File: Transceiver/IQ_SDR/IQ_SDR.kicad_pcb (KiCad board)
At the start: 2 copper layers, 100 x 100 mm, 116 parts, among them CON1 SJ1-3523N, J1 ANT, J10 LO_I, J11 LO_Q, J12 GNDA, J13 I_IN, J14 Q_IN, J15 +5V, J16 4.3V, J17 I_OUT, J18 Q_OUT, J19 Conn_01x01_Male, J2 GND, J20 Conn_01x01_Male, J3 V_IN pin header, J4 GND, J5 V_IN, J6 FIL_O, J7 CLK1, J8 CLK2, J9 CLK0, P1 BNC, P2 SMA, Q1 MMBT2222A-TP, T1 Transformer_1P_SS, U1 FST3253, U2 Si5351A-B-GT, U3 TS5A23157, U4 LM4562 or LT6231, U5 74ALVC74D, Y1 CX3225

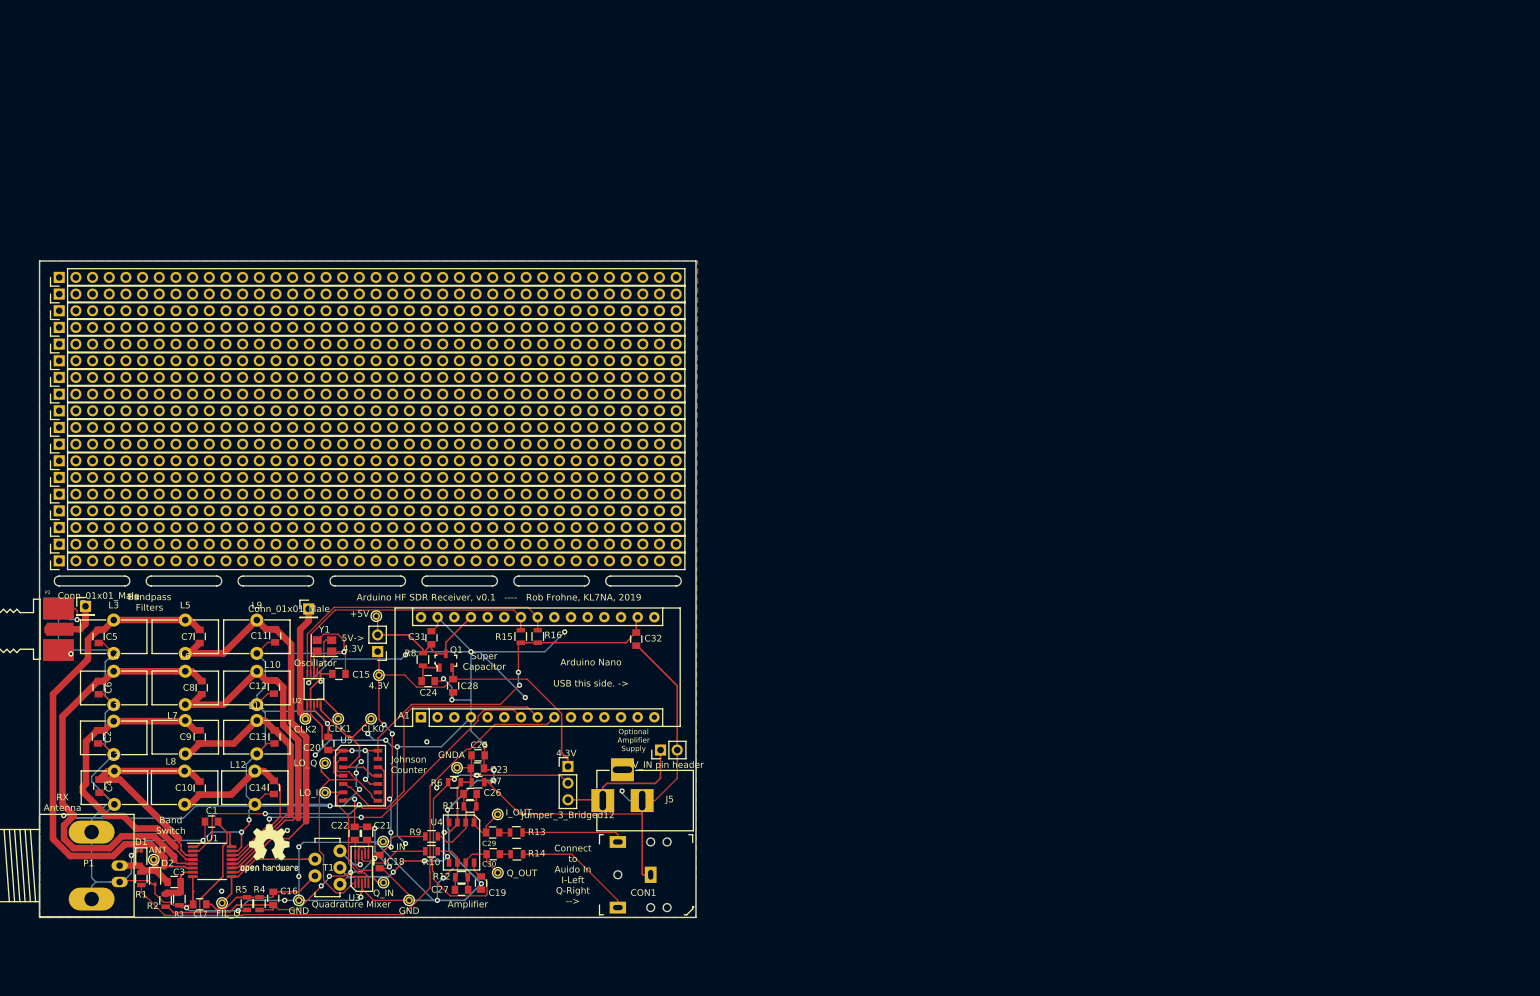
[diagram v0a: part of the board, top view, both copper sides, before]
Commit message: Further change to schematic and moving simulations
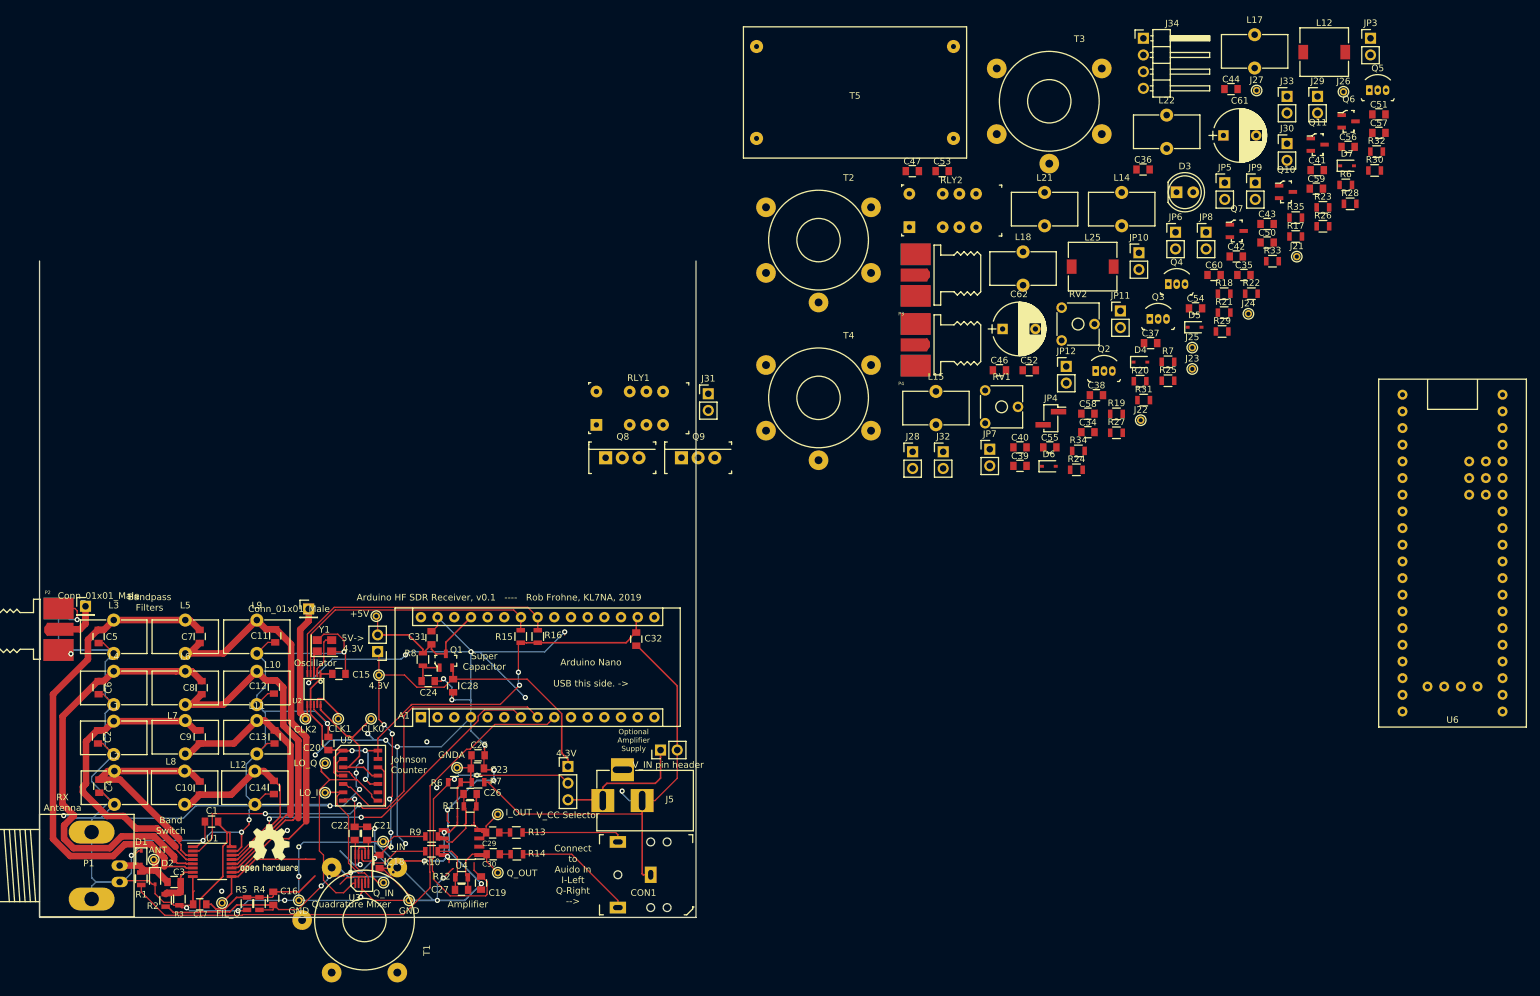
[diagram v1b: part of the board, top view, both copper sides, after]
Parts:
- removed REF** (x18): Pin_Header_Straight_1x38_Pitch2.54mm, Pin_Headers:Pin_Header_Straight_1x38_Pitch2.54mm
- added C34: 82pF, Capacitors_SMD:C_0805, F.Cu at (254.7, 71.1)
- added C35: 1uF, Capacitors_SMD:C_0805, F.Cu at (278.5, 47.1)
- added C36: 10uF, Capacitors_SMD:C_0805, F.Cu at (263.1, 31.1)
- added C37: 1u, Capacitors_SMD:C_0805, F.Cu at (264.3, 57.5)
- added C38: 510pF, Capacitors_SMD:C_0805, F.Cu at (256.0, 65.4)
- added C39: 330pF, Capacitors_SMD:C_0805, F.Cu at (244.4, 76.2)
- added C40: 0.1uF, Capacitors_SMD:C_0805, F.Cu at (244.4, 73.4)
- added C41: 220pF, Capacitors_SMD:C_0805, F.Cu at (289.6, 31.2)
- added C42: 680pF, Capacitors_SMD:C_0805, F.Cu at (277.3, 44.3)
- added C43: 330pF, Capacitors_SMD:C_0805, F.Cu at (282.0, 39.4)
- added C44: 220pF, Capacitors_SMD:C_0805, F.Cu at (276.5, 18.8)
- added C46: 180pF, Capacitors_SMD:C_0805, F.Cu at (241.2, 61.6)
- added C47: 82pF, Capacitors_SMD:C_0805, F.Cu at (228.0, 31.3)
- added C50: 0.1uF, Capacitors_SMD:C_0805, F.Cu at (282.0, 42.2)
- added C51: 0.1uF, Capacitors_SMD:C_0805, F.Cu at (299.0, 22.7)
- added C52: 0.1uF, Capacitors_SMD:C_0805, F.Cu at (245.8, 61.6)
- added C53: 0.1uF, Capacitors_SMD:C_0805, F.Cu at (232.5, 31.3)
- added C54: 0.1uF, Capacitors_SMD:C_0805, F.Cu at (271.1, 52.2)
- added C55: 0.1uF, Capacitors_SMD:C_0805, F.Cu at (248.9, 73.4)
- added C56: 0.1uF, Capacitors_SMD:C_0805, F.Cu at (294.3, 27.6)
- added C57: 0.1uF, Capacitors_SMD:C_0805, F.Cu at (299.0, 25.5)
- added C58: 0.1uF, Capacitors_SMD:C_0805, F.Cu at (254.7, 68.3)
- added C59: 0.1uF, Capacitors_SMD:C_0805, F.Cu at (289.5, 34.0)
- added C60: 0.1uF, Capacitors_SMD:C_0805, F.Cu at (273.9, 47.1)
- added C61: 470uF, Capacitors_THT:CP_Radial_D8.0mm_P5.00mm, F.Cu at (275.3, 25.9)
- added C62: 470uF, Capacitors_THT:CP_Radial_D8.0mm_P5.00mm, F.Cu at (241.7, 55.4)
- added D3: LED_Solid, LEDs:LED_D5.0mm, F.Cu at (268.2, 34.5)
- added D4: 1N914, Diodes_SMD:D_SOD-323, F.Cu at (262.7, 60.4)
- added D5: 1N914, Diodes_SMD:D_SOD-323, F.Cu at (271.0, 55.1)
- added D6: 1N914, Diodes_SMD:D_SOD-323, F.Cu at (248.8, 76.3)
- added D7: 1N914, Diodes_SMD:D_SOD-323, F.Cu at (294.2, 30.5)
- added J21: V_CC, Connectors:PINTST, F.Cu at (286.5, 44.3)
- added J22: Ba, Connectors:PINTST, F.Cu at (262.8, 69.3)
- added J23: Bb, Connectors:PINTST, F.Cu at (270.6, 61.4)
- added J24: Cb, Connectors:PINTST, F.Cu at (279.2, 53.0)
- added J25: Ca, Connectors:PINTST, F.Cu at (270.6, 58.2)
- added J26: Gb, Connectors:PINTST, F.Cu at (293.6, 19.2)
- added J27: Ga, Connectors:PINTST, F.Cu at (280.4, 19.0)
- added J28: Conn_01x02_Female, Socket_Strips:Socket_Strip_Straight_1x02_Pitch2.54mm, F.Cu at (228.0, 74.1)
- added J29: Conn_01x02_Female, Socket_Strips:Socket_Strip_Straight_1x02_Pitch2.54mm, F.Cu at (289.7, 19.9)
- added J30: Conn_01x02_Female, Socket_Strips:Socket_Strip_Straight_1x02_Pitch2.54mm, F.Cu at (285.0, 27.1)
- added J31: Conn_01x02_Female, Socket_Strips:Socket_Strip_Straight_1x02_Pitch2.54mm, F.Cu at (196.9, 65.2)
- added J32: Conn_01x02_Female, Socket_Strips:Socket_Strip_Straight_1x02_Pitch2.54mm, F.Cu at (232.7, 74.1)
- added J33: Conn_01x02_Female, Socket_Strips:Socket_Strip_Straight_1x02_Pitch2.54mm, F.Cu at (285.0, 19.9)
- added J34: Conn_01x04_Male, Pin_Headers:Pin_Header_Angled_1x04_Pitch2.54mm, F.Cu at (263.2, 11.1)
- added JP10: BP_2, Pin_Headers:Pin_Header_Straight_1x02_Pitch2.54mm, F.Cu at (262.5, 43.8)
- added JP11: Tx filter disconnect, Pin_Headers:Pin_Header_Straight_1x02_Pitch2.54mm, F.Cu at (259.7, 52.6)
- added JP12: 40m Filter Bypass, Pin_Headers:Pin_Header_Straight_1x02_Pitch2.54mm, F.Cu at (251.4, 61.1)
- added JP3: Ground loop mitigation for the Arduino, Pin_Headers:Pin_Header_Straight_1x02_Pitch2.54mm, F.Cu at (297.8, 11.1)
- added JP4: Ground loop mitigation for the RX antenna, Pin_Headers:Pin_Header_Straight_1x02_Pitch2.00mm_SMD_Pin1Right, F.Cu at (249.1, 69.0)
- added JP5: T2 bypass, Pin_Headers:Pin_Header_Straight_1x02_Pitch2.54mm, F.Cu at (275.6, 33.1)
- added JP6: T2 bypass, Pin_Headers:Pin_Header_Straight_1x02_Pitch2.54mm, F.Cu at (268.1, 40.6)
- added JP7: V_IN ground loop mitigation, Pin_Headers:Pin_Header_Straight_1x02_Pitch2.54mm, F.Cu at (239.8, 73.7)
- added JP8: Ground loop mitigation for audio, Pin_Headers:Pin_Header_Straight_1x02_Pitch2.54mm, F.Cu at (272.7, 40.6)
- added JP9: BP_1, Pin_Headers:Pin_Header_Straight_1x02_Pitch2.54mm, F.Cu at (280.2, 33.1)
- added L12: 300uH, Inductors_SMD:L_7.3x7.3_H4.5, F.Cu at (290.7, 13.2)
- added L14: 590nH, Inductors_THT:L_Toroid_Vertical_L10.0mm_W5.0mm_P5.08mm, F.Cu at (259.9, 34.6)
- added L15: 2.4uH, Inductors_THT:L_Toroid_Vertical_L10.0mm_W5.0mm_P5.08mm, F.Cu at (231.6, 64.9)
- added L17: 1.7uH, Inductors_THT:L_Toroid_Vertical_L10.0mm_W5.0mm_P5.08mm, F.Cu at (280.1, 10.5)
- added L18: 910nH, Inductors_THT:L_Toroid_Vertical_L10.0mm_W5.0mm_P5.08mm, F.Cu at (244.8, 43.6)
- added L21: 1.24uH, Inductors_THT:L_Toroid_Vertical_L10.0mm_W5.0mm_P5.08mm, F.Cu at (248.1, 34.6)
- added L22: 590nH, Inductors_THT:L_Toroid_Vertical_L10.0mm_W5.0mm_P5.08mm, F.Cu at (266.7, 22.8)
- added L25: 300uH, Inductors_SMD:L_7.3x7.3_H4.5, F.Cu at (255.4, 45.9)
- added P3: SMA, SMA:SMA_EDGE, F.Cu at (237.4, 47.1)
- added P4: SMA, SMA:SMA_EDGE, F.Cu at (237.4, 57.8)
- added Q10: MMBT2222A-TP, digikey-footprints:SOT-23-3, F.Cu at (284.9, 34.5)
- added Q11: MMBT2222A-TP, digikey-footprints:SOT-23-3, F.Cu at (289.7, 27.3)
- added Q2: 2N3904, digikey-footprints:TO-92-3, F.Cu at (255.9, 61.8)
- added Q3: 2N3904, digikey-footprints:TO-92-3, F.Cu at (264.1, 53.8)
- added Q4: 2N3904, digikey-footprints:TO-92-3, F.Cu at (267.0, 48.5)
- added Q5: 2N3904, digikey-footprints:TO-92-3, F.Cu at (297.6, 19.0)
- added Q6: MMBT2222A-TP, digikey-footprints:SOT-23-3, F.Cu at (294.4, 23.7)
- added Q7: MMBT2222A-TP, digikey-footprints:SOT-23-3, F.Cu at (277.4, 40.4)
- added Q8: IRF510PBF, digikey-footprints:TO-220-3, F.Cu at (181.2, 75.0)
- added Q9: IRF510PBF, digikey-footprints:TO-220-3, F.Cu at (192.8, 75.0)
- added R17: 100, Resistors_SMD:R_0805, F.Cu at (286.4, 41.3)
- added R18: 100, Resistors_SMD:R_0805, F.Cu at (275.5, 50.0)
- added R19: 22, Resistors_SMD:R_0805, F.Cu at (259.1, 68.3)
- added R20: 22, Resistors_SMD:R_0805, F.Cu at (262.7, 63.3)
- added R21: 1k, Resistors_SMD:R_0805, F.Cu at (275.5, 52.9)
- added R22: 1k, Resistors_SMD:R_0805, F.Cu at (279.6, 50.0)
- added R23: 22, Resistors_SMD:R_0805, F.Cu at (290.5, 36.8)
- added R24: 22, Resistors_SMD:R_0805, F.Cu at (253.0, 76.8)
- added R25: 2.2, Resistors_SMD:R_0805, F.Cu at (266.9, 63.2)
- added R26: 0, Resistors_SMD:R_0805, F.Cu at (290.5, 39.7)
- added R27: 0, Resistors_SMD:R_0805, F.Cu at (259.1, 71.2)
- added R28: 500, Resistors_SMD:R_0805, F.Cu at (294.7, 36.3)
- added R29: 47, Resistors_SMD:R_0805, F.Cu at (275.2, 55.7)
- added R30: 47, Resistors_SMD:R_0805, F.Cu at (298.4, 31.2)
- added R31: 220, Resistors_SMD:R_0805, F.Cu at (263.2, 66.2)
- added R32: 220, Resistors_SMD:R_0805, F.Cu at (298.7, 28.3)
- added R33: 4.7k, Resistors_SMD:R_0805, F.Cu at (282.8, 45.0)
- added R34: 4.7k, Resistors_SMD:R_0805, F.Cu at (253.3, 73.9)
- added R35: 1.6k, Resistors_SMD:R_0805, F.Cu at (286.4, 38.4)
- added R6: 2k, Resistors_SMD:R_0805, F.Cu at (294.0, 33.4)
- added R7: 27k, Resistors_SMD:R_0805, F.Cu at (266.9, 60.4)
- added RLY1: TX2SA-L-3V-Z, IQ_SDR:TX2SA-L-3V-Z, F.Cu at (179.8, 64.9)
- added RLY2: TX2SA-L-3V-Z, IQ_SDR:TX2SA-L-3V-Z, F.Cu at (227.5, 34.8)
- added RV1: 10k, Potentiometers:Potentiometer_Trimmer_ACP_CA6v_Horizontal, F.Cu at (239.1, 69.7)
- added RV2: 10k, Potentiometers:Potentiometer_Trimmer_ACP_CA6v_Horizontal, F.Cu at (250.7, 57.1)
- added T2: Transformer_1P_1S, IQ_SDR:Transformer_Toroid_Tapped_Secondary_Horizontal_D14.0mm_Amidon-T50, F.Cu at (205.7, 46.8)
- added T3: Transformer_1P_1S, IQ_SDR:Transformer_Toroid_Tapped_Secondary_Horizontal_D14.0mm_Amidon-T50, F.Cu at (240.8, 25.7)
- added T4: Transformer_SP_1S, IQ_SDR:Transformer_Toroid_Tapped_Secondary_Horizontal_D14.0mm_Amidon-T50, F.Cu at (205.7, 70.8)
- added T5: BN43-6802, IQ_SDR:BN43-6802, F.Cu at (219.2, 19.3)
- added U6: Blue Pill, blue_pill:BLUEPILL, F.Cu at (310.2, 89.5)
- C21, C22: value 0.1uF -> 0.02uF
- C26, C27: value 2200pF -> 50pF
- JP2: value Jumper_3_Bridged12 -> V_CC Selector
- L10: value 497nH -> 626nH
- L11: value 1uH -> 1.7uH
- L9: value 232nH -> 256nH
- R10, R9: value 10 -> 50
- R11, R12: value 1.0k -> 13k
- T1: footprint SMA:4_to_1_Transmission_Line_TransformerTHT -> IQ_SDR:Transformer_Toroid_Tapped_Secondary_Horizontal_D14.0mm_Amidon-T50
- U1: value FST3253 -> FST3253 or TS3A5017
- U4: footprint SMA:DMP8 -> Housings_SOIC:SOIC-8_3.9x4.9mm_Pitch1.27mm
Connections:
- A1 pad 29: GND -> /D_GND
- A1 pad 4: GND -> /D_GND
- C16 pad 2: Net-(C16-Pad2) -> GNDA
- C17 pad 1: Net-(C16-Pad2) -> GNDA
- C23 pad 2: GNDA -> Net-(C23-Pad2)
- C3 pad 1: /RF_IN -> Net-(C3-Pad1)
- C4 pad 1: Net-(C10-Pad2) -> Net-(C4-Pad1)
- C7 pad 2: Net-(C5-Pad1) -> Net-(C7-Pad2)
- C8 pad 2: Net-(C6-Pad1) -> Net-(C8-Pad2)
- C9 pad 2: Net-(C2-Pad1) -> Net-(C9-Pad2)
- CON1 pad 1: GND -> Net-(CON1-Pad1)
- D1 pad 2: /RF_IN -> Net-(C3-Pad1)
- D2 pad 1: /RF_IN -> Net-(C3-Pad1)
- J1 pad 1: /RF_IN -> Net-(C3-Pad1)
- J3 pad 2: GND -> Net-(J3-Pad2)
- J5 pad 2: GND -> Net-(J3-Pad2)
- L1 pad 2: GND -> GNDA
- L10 pad 2: GND -> GNDA
- L11 pad 2: GND -> GNDA
- L2 pad 1: Net-(C10-Pad2) -> Net-(C4-Pad1)
- L2 pad 2: GND -> GNDA
- L3 pad 2: GND -> GNDA
- L4 pad 2: GND -> GNDA
- L5 pad 2: Net-(C11-Pad1) -> Net-(C7-Pad2)
- L6 pad 2: Net-(C12-Pad1) -> Net-(C8-Pad2)
- L7 pad 2: Net-(C13-Pad1) -> Net-(C9-Pad2)
- L8 pad 1: Net-(C10-Pad2) -> Net-(C4-Pad1)
- L8 pad 2: Net-(C10-Pad1) -> Net-(C10-Pad2)
- L9 pad 2: GND -> GNDA
- P1 pad 1: /RF_IN -> Net-(P1-Pad1)
- P1 pad 2: GND -> Net-(P1-Pad2)
- R1 pad 1: /RF_IN -> Net-(C3-Pad1)
- R4 pad 1: Net-(C16-Pad2) -> GNDA
- R5 pad 2: Net-(C16-Pad2) -> GNDA
- T1 pad 1: Net-(C16-Pad2) -> GNDA
- T1 pad 3: Net-(T1-Pad3) -> Net-(R26-Pad2)
- T1 pad 5: Net-(T1-Pad5) -> Net-(R27-Pad2)
- U1 pad 3: Net-(C10-Pad2) -> Net-(C4-Pad1)
- U1 pad 9: Net-(J6-Pad1) -> Net-(JP9-Pad1)
- U3 pad 2: Net-(T1-Pad5) -> Net-(R27-Pad1)
- U3 pad 4: Net-(T1-Pad5) -> Net-(R27-Pad1)
- U3 pad 7: Net-(T1-Pad3) -> Net-(R26-Pad1)
- U3 pad 9: Net-(T1-Pad3) -> Net-(R26-Pad1)
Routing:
- net Net-(C16-Pad2): track 19.3 -> 0.00 mm
- net GNDA: track 40.6 -> 60.0 mm
- net Net-(T1-Pad3): track 8.53 -> 0.00 mm, vias 1 -> 0
- net Net-(R26-Pad1): track 0.00 -> 8.53 mm, vias 0 -> 1
- net Net-(T1-Pad5): track 6.86 -> 0.00 mm
- net Net-(R27-Pad1): track 0.00 -> 6.86 mm
- removed copper zone on B.Cu, net GND
- removed copper zone on F.Cu, net GND
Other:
- outline, holes or cut-outs redrawn

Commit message: PCB initial design
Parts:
- removed the L12 at (127.8, 122.7)
- removed the R6 at (158.2, 124.4)
- removed the R7 at (161.8, 124.4)
- removed REF***: OSHW-Logo2_36.5x30mm_SilkScreen, Symbols:OSHW-Logo2_36.5x30mm_SilkScreen
- removed REF***: OSHW-Logo2_9.8x8mm_SilkScreen, Symbols:OSHW-Logo2_9.8x8mm_SilkScreen
- added JP13: QRP, Pin_Headers:Pin_Header_Straight_1x02_Pitch2.54mm, F.Cu at (106.0, 75.5)
- added JP14: QRP, Pin_Headers:Pin_Header_Straight_1x02_Pitch2.54mm, F.Cu at (135.0, 75.8)
- added P5: SMA, SMA:SMA_EDGE, F.Cu at (88.8, 83.2)
- J34: footprint Pin_Headers:Pin_Header_Angled_1x04_Pitch2.54mm -> Pin_Headers:Pin_Header_Straight_1x04_Pitch2.54mm
- JP4: footprint Pin_Headers:Pin_Header_Straight_1x02_Pitch2.00mm_SMD_Pin1Right -> Pin_Headers:Pin_Header_Straight_1x02_Pitch2.54mm
- R26, R27: footprint Resistors_SMD:R_0805 -> Socket_Strips:Socket_Strip_Straight_1x02_Pitch2.54mm
- T1, T4: footprint IQ_SDR:Transformer_Toroid_Tapped_Secondary_Horizontal_D14.0mm_Amidon-T50 -> IQ_SDR:T50-2_vertical_5_pin
- T2, T3: footprint IQ_SDR:Transformer_Toroid_Tapped_Secondary_Horizontal_D14.0mm_Amidon-T50 -> IQ_SDR:T50-2_vertical_4_pin
- moved Q5 198.0 mm to (111.8, 87.2), turned to 270 degrees
- moved R23 192.6 mm to (107.5, 96.8), turned to 180 degrees
- moved L12 191.9 mm to (102.2, 49.5), turned to 180 degrees
- moved JP9 191.0 mm to (122.2, 140.5), turned to 270 degrees
- moved C57 190.7 mm to (110.0, 50.8)
- moved J21 190.3 mm to (96.2, 47.2)
- moved J27 187.6 mm to (96.2, 54.8)
- moved C51 186.1 mm to (125.2, 89.2), turned to 90 degrees
- moved J29 181.4 mm to (152.2, 138.2), turned to 90 degrees
- moved R17 181.2 mm to (113.5, 95.8), turned to 270 degrees
- moved R26 178.8 mm to (144.8, 143.2), turned to 270 degrees
- moved C41 178.3 mm to (122.2, 92.5)
- moved J33 176.5 mm to (158.5, 143.0), turned to 90 degrees
- moved C61 175.8 mm to (104.2, 66.5), turned to 180 degrees
- moved C60 175.0 mm to (100.8, 72.5), turned to 180 degrees
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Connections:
- net Net-(C34-Pad1) renamed /Rfe
- net Net-(C35-Pad2) renamed /RFc
- net Net-(C38-Pad1) renamed /RFg
- net Net-(C39-Pad1) renamed /RFf
- net Net-(C42-Pad1) renamed /RFk
- net Net-(C43-Pad1) renamed /RFj
- net Net-(C46-Pad1) renamed /RFh
- net Net-(C47-Pad1) renamed /RFd
- net Net-(P1-Pad1) renamed /RFm
- net Net-(P1-Pad2) renamed /RFb
- net Net-(P4-Pad2) renamed /RFa
- A1 pad 25: (no net) -> /TX_BAND
- A1 pad 26: (no net) -> /ANT_RLY
- L12 pad 1: Net-(L12-Pad1) -> /PA_V_CCb
- L25 pad 1: Net-(L25-Pad1) -> /PA_V_CCc
- Q3 pad 1: Net-(C44-Pad1) -> Net-(Q3-Pad1)
- Q3 pad 3: Net-(Q3-Pad3) -> Net-(C44-Pad1)
- Q5 pad 1: Net-(C44-Pad1) -> Net-(Q5-Pad1)
- Q5 pad 3: Net-(Q5-Pad3) -> Net-(C44-Pad1)
- Q8 pad 2: Net-(Q8-Pad2) -> /PA_V_CCb
- Q9 pad 2: Net-(Q9-Pad2) -> /PA_V_CCc
- R15 pad 1: /SCL -> /SDA
- R16 pad 1: /SDA -> /SCL
- R20 pad 1: Net-(Q3-Pad3) -> Net-(Q3-Pad1)
- R24 pad 1: Net-(Q5-Pad3) -> Net-(Q5-Pad1)
- R31 pad 1: Net-(L12-Pad1) -> /PA_V_CCb
- R32 pad 1: Net-(L25-Pad1) -> /PA_V_CCc
- T3 pad 1: Net-(J7-Pad1) -> GND
- T3 pad 2: GND -> Net-(J7-Pad1)
- T3 pad 3: Net-(C51-Pad2) -> Net-(C50-Pad2)
- T3 pad 4: Net-(C50-Pad2) -> Net-(C51-Pad2)
- T4 pad 1: Net-(C41-Pad1) -> Net-(C44-Pad1)
- T4 pad 3: Net-(C44-Pad1) -> Net-(C41-Pad1)
- T4 pad 4: Net-(C55-Pad2) -> Net-(JP13-Pad1)
- T4 pad 5: Net-(C54-Pad2) -> Net-(JP14-Pad1)
- T5 pad 1: Net-(Q8-Pad2) -> /PA_V_CCb
- T5 pad 2: Net-(Q9-Pad2) -> /PA_V_CCc
- U6 pad PB6: (no net) -> /SCL
- U6 pad PB7: (no net) -> /SDA
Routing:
- net V_CC: track 50.2 -> 221.7 mm, vias 2 -> 5
- net GNDA: track 60.0 -> 192.9 mm, vias 4 -> 9
- net Net-(C3-Pad1): track 0.00 -> 130.1 mm, vias 0 -> 4
- net /D_GND: track 0.00 -> 112.0 mm, vias 0 -> 3
- net +3V3: track 91.8 -> 198.6 mm, vias 5 -> 8
- net +4.3V: track 138.2 -> 241.8 mm, vias 9 -> 10
- net /RFa: track 0.00 -> 101.5 mm, vias 0 -> 3
- net Net-(C55-Pad1): track 0.00 -> 67.1 mm, vias 0 -> 2
- net /Rfe: track 0.00 -> 65.0 mm, vias 0 -> 1
- net Net-(JP10-Pad1): track 0.00 -> 62.1 mm, vias 0 -> 2
- net Net-(JP14-Pad1): track 0.00 -> 58.3 mm, vias 0 -> 2
- net Net-(D7-Pad2): track 0.00 -> 57.3 mm
- net GND: track 663.8 -> 718.4 mm, vias 46 -> 49
- net +5V: track 23.7 -> 74.5 mm, vias 0 -> 4
- net Net-(C54-Pad1): track 0.00 -> 49.5 mm, vias 0 -> 1
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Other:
- net class 2A added: clearance 0.2, trace_width 2, via_dia 2, via_drill 0.4
- net class 50 Ohms added: clearance 0.2, trace_width 1, via_dia 1, via_drill 0.4
- net class RF out added: clearance 0.2, trace_width 0.25, via_dia 0.8, via_drill 0.4
- board text removed: "4.3V"
- board text removed: "5V-> 4.3V"
- board text removed: "Amplifier"
- board text removed: "Arduino HF SDR Receiver"
- board text removed: "Arduino HF SDR Receiver, v0.1 ---- Rob Frohne, KL7NA, 2019"
- board text removed: "Arduino Nano USB this side. ->"
- board text removed: "Band Switch"
- board text removed: "Bandpass Filters"
- board text removed: "Connect to Auido In I-Left Q-Right -->"
- board text removed: "Johnson Counter"
- board text removed: "Optional Amplifier Supply"
- board text removed: "Oscillator"
- board text removed: "Quadrature Mixer"
- board text removed: "RX Antenna"
- board text removed: "Super Capacitor"
- board text removed: "v0.1 Rob Frohne, KL7NA"

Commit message: More edits to the PCB
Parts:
- added REF***: OSHW-Logo2_36.5x30mm_SilkScreen, Symbols:OSHW-Logo2_36.5x30mm_SilkScreen, B.Cu at (148.0, 99.1)
- J19: value Conn_01x01_Male -> CLK2
- J20: value Conn_01x01_Male -> SMA
- J3: value V_IN pin header -> V_IN
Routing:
- net GNDA: track 192.9 -> 260.5 mm, vias 9 -> 15
- added copper zone on B.Cu, net GND
- added copper zone on F.Cu, net GND
- added copper zone on B.Cu, net GNDA
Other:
- board text added: "IQ_SDR HF Digital Transceiver version 0.2 KL7NA 4/26/2020"
